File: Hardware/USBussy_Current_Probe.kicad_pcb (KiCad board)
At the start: 4 copper layers, 33.5 x 30 mm, 29 parts, among them J1 USB_C_Receptacle_USB2.0, J2 Mobo header, J3 CFG_OPT1, J4 CFG_COM, J5 CFG_OPT2, J6 USB_A, J7 Jumper holder, J8 MEAS, Q1 RE1C002UN, Q2 RE1C002UN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

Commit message: Add texts on board and export
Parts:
- added SYM1: ~, leptunKicadLib:AMOGUS, B.Cu at (36.6, 83.1)
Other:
- board text added: "USBussy Current Probe Alex Voinea https://github.com/leptun"
- board text added: "rev ${REVISION} ${ISSUE_DATE}"
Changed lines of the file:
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@@
       (plot_on_all_layers_selection 0x0000000_00000000)
       (disableapertmacros false)
-      (usegerberextensions false)
-      (usegerberattributes true)
-      (usegerberadvancedattributes true)
-      (creategerberjobfile true)
+      (usegerberextensions true)
+      (usegerberattributes false)
+      (usegerberadvancedattributes false)
+      (creategerberjobfile false)
       (dashed_line_dash_ratio 12.000000)
       (dashed_line_gap_ratio 3.000000)
@@
       (plotinvisibletext false)
       (sketchpadsonfab false)
-      (subtractmaskfromsilk false)
+      (subtractmaskfromsilk true)
       (outputformat 1)
       (mirror false)
-      (drillshape 1)
+      (drillshape 0)
       (scaleselection 1)
-      (outputdirectory "")
+      (outputdirectory "out/")
     )
   )
@@
     (fp_line (start 1 0.625) (end -1 0.625)
       (stroke (width 0.1) (type solid)) (layer "F.Fab"))
-    (pad "1" smd roundrect (at -0.9125 0 180) (size 1.025 1.4) (layers "F.Cu" "F.Paste" "F.Mask") (roundrect_rratio 0.243902)
+    (pad "1" smd roundrect (at -0.9125 0 180) (size 1.025 1.4) (layers "F.Cu" "F.Paste" "F.Mask") (roundrect_rratio 0.243902439)
       (net 6 "Net-(D2-A)") (pintype "passive"))
-    (pad "2" smd roundrect (at 0.9125 0 180) (size 1.025 1.4) (layers "F.Cu" "F.Paste" "F.Mask") (roundrect_rratio 0.243902)
+    (pad "2" smd roundrect (at 0.9125 0 180) (size 1.025 1.4) (layers "F.Cu" "F.Paste" "F.Mask") (roundrect_rratio 0.243902439)
       (net 1 "+5V") (pintype "passive"))
     (model "${KICAD6_3DMODEL_DIR}/Resistor_SMD.3dshapes/R_0805_2012Metric.wrl"
@@
     (fp_line (start 1 0.625) (end -1 0.625)
       (stroke (width 0.1) (type solid)) (layer "F.Fab"))
-    (pad "1" smd roundrect (at -0.9125 0 180) (size 1.025 1.4) (layers "F.Cu" "F.Paste" "F.Mask") (roundrect_rratio 0.243902)
+    (pad "1" smd roundrect (at -0.9125 0 180) (size 1.025 1.4) (layers "F.Cu" "F.Paste" "F.Mask") (roundrect_rratio 0.243902439)
       (net 4 "Net-(D1-A)") (pintype "passive"))
-    (pad "2" smd roundrect (at 0.9125 0 180) (size 1.025 1.4) (layers "F.Cu" "F.Paste" "F.Mask") (roundrect_rratio 0.243902)
+    (pad "2" smd roundrect (at 0.9125 0 180) (size 1.025 1.4) (layers "F.Cu" "F.Paste" "F.Mask") (roundrect_rratio 0.243902439)
       (net 1 "+5V") (pintype "passive"))
     (model "${KICAD6_3DMODEL_DIR}/Resistor_SMD.3dshapes/R_0805_2012Metric.wrl"
@@
     (fp_line (start 1.6 1.25) (end -1.6 1.25)
       (stroke (width 0.1) (type solid)) (layer "F.Fab"))
-    (pad "1" smd roundrect (at -1.475 0 180) (size 1.15 2.7) (layers "F.Cu" "F.Paste" "F.Mask") (roundrect_rratio 0.217391)
+    (pad "1" smd roundrect (at -1.475 0 180) (size 1.15 2.7) (layers "F.Cu" "F.Paste" "F.Mask") (roundrect_rratio 0.2173913043)
       (net 2 "GND") (pintype "passive"))
-    (pad "2" smd roundrect (at 1.475 0 180) (size 1.15 2.7) (layers "F.Cu" "F.Paste" "F.Mask") (roundrect_rratio 0.217391)
+    (pad "2" smd roundrect (at 1.475 0 180) (size 1.15 2.7) (layers "F.Cu" "F.Paste" "F.Mask") (roundrect_rratio 0.2173913043)
       (net 7 "/USB_C_VBUS") (pintype "passive"))
     (model "${KICAD6_3DMODEL_DIR}/Capacitor_SMD.3dshapes/C_1210_3225Metric.wrl"
@@
     )
   )
+  (footprint "leptunKicadLib:AMOGUS" (layer "B.Cu")
+    (at 36.6014 83.0834 -90)
+    (property "Sheetfile" "USBussy_Current_Probe.kicad_sch")
+    (property "Sheetname" "")
+    (property "Sim.Enable" "0")
+    (property "exclude_from_bom" "")
+    (property "ki_description" "Open Hardware logo, small")
+    (property "ki_keywords" "Logo")
+    (attr through_hole exclude_from_bom)
+    (fp_text reference "SYM1" (at 0 -0.5 -270) (layer "B.SilkS") hide
+        (effects (font (size 1 1) (thickness 0.15)) (justify mirror))
+    )
+    (fp_text value "~" (at 0 0.5 -270) (layer "B.Fab")
+        (effects (font (size 1 1) (thickness 0.15)) (justify mirror))
+    )
+    (fp_curve (pts (xy -4.990555 -4.274239) (xy -4.479356 -3.251843) (xy -4.452111 -1.799887) (xy -4.270555 -0.674239))
+      (stroke (width 0.2) (type solid)) (layer "B.SilkS"))
+    (fp_curve (pts (xy -4.270555 -0.674239) (xy -4.025142 0.84732) (xy -3.680852 2.332061) (xy -3.230555 3.805761))
+      (stroke (width 0.2) (type solid)) (layer "B.SilkS"))
+    (fp_curve (pts (xy -3.870555 -5.634239) (xy -7.87736 -6.404779) (xy -8.612551 -3.469351) (xy -4.990555 -4.274239))
+      (stroke (width 0.2) (type solid)) (layer "B.SilkS"))
+    (fp_curve (pts (xy -3.230555 3.805761) (xy -3.075315 4.313819) (xy -2.616498 6.952463) (xy -1.550555 7.005761))
+      (stroke (width 0.2) (type solid)) (layer "B.SilkS"))
+    (fp_curve (pts (xy -2.271776 4.382116) (xy -2.269771 4.961755) (xy -1.098997 5.53735) (xy 0.069772 5.533306))
+      (stroke (width 0.2) (type solid)) (layer "B.SilkS"))
+    (fp_curve (pts (xy -1.550555 7.005761) (xy 0.209624 7.09377) (xy 0.753252 7.074619) (xy 2.049445 6.685761))
+      (stroke (width 0.2) (type solid)) (layer "B.SilkS"))
+    (fp_curve (pts (xy -0.830555 -6.514239) (xy -0.961599 -4.941714) (xy 0.912248 -5.749496) (xy 1.169445 -5.314239))
+      (stroke (width 0.2) (type solid)) (layer "B.SilkS"))
+    (fp_curve (pts (xy 0.06175 3.214751) (xy -1.107019 3.218795) (xy -2.273782 3.802477) (xy -2.271776 4.382116))
+      (stroke (width 0.2) (type solid)) (layer "B.SilkS"))
+    (fp_curve (pts (xy 0.069772 5.533306) (xy 1.238541 5.529262) (xy 2.405304 4.945579) (xy 2.403298 4.365941))
+      (stroke (width 0.2) (type solid)) (layer "B.SilkS"))
+    (fp_curve (pts (xy 0.449445 -2.114239) (xy -5.606765 -1.357213) (xy -0.20818 -4.929937) (xy -3.870555 -5.634239))
+      (stroke (width 0.2) (type solid)) (layer "B.SilkS"))
+    (fp_curve (pts (xy 1.089445 -2.434239) (xy 0.894047 -2.297461) (xy 0.686117 -2.143823) (xy 0.449445 -2.114239))
+      (stroke (width 0.2) (type solid)) (layer "B.SilkS"))
+    (fp_curve (pts (xy 1.169445 -5.314239) (xy 1.353719 -5.002391) (xy 1.746386 -2.894098) (xy 1.089445 -2.434239))
+      (stroke (width 0.2) (type solid)) (layer "B.SilkS"))
+    (fp_curve (pts (xy 1.489445 -7.154239) (xy 1.341106 -7.159025) (xy -0.768282 -7.261512) (xy -0.830555 -6.514239))
+      (stroke (width 0.2) (type solid)) (layer "B.SilkS"))
+    (fp_curve (pts (xy 2.049445 6.685761) (xy 3.34614 6.296752) (xy 3.868407 3.776144) (xy 3.969445 2.765761))
+      (stroke (width 0.2) (type solid)) (layer "B.SilkS"))
+    (fp_curve (pts (xy 2.403298 4.365941) (xy 2.401293 3.786302) (xy 1.230519 3.210707) (xy 0.06175 3.214751))
+      (stroke (width 0.2) (type solid)) (layer "B.SilkS"))
+    (fp_curve (pts (xy 2.449445 -6.994239) (xy 2.131331 -7.057862) (xy 1.813691 -7.14378) (xy 1.489445 -7.154239))
+      (stroke (width 0.2) (type solid)) (layer "B.SilkS"))
+    (fp_curve (pts (xy 3.969445 2.765761) (xy 4.070589 1.754319) (xy 4.149047 0.740451) (xy 4.209445 -0.274239))
+      (stroke (width 0.2) (type solid)) (layer "B.SilkS"))
+    (fp_curve (pts (xy 4.209445 -0.274239) (xy 4.282401 -1.499896) (xy 4.369445 -2.726414) (xy 4.369445 -3.954239))
+      (stroke (width 0.2) (type solid)) (layer "B.SilkS"))
+    (fp_curve (pts (xy 4.369445 -3.954239) (xy 4.369445 -5.989742) (xy 4.386831 -6.606762) (xy 2.449445 -6.994239))
+      (stroke (width 0.2) (type solid)) (layer "B.SilkS"))
+  )
   (gr_rect (start 29.083 58.039) (end 62.611 88.011)
     (stroke (width 0.1) (type default)) (fill none) (layer "Edge.Cuts"))
+  (gr_text "rev ${REVISION}\n${ISSUE_DATE}" (at 41.6052 86.8426) (layer "B.SilkS")
+    (effects (font (size 0.8 0.8) (thickness 0.12)) (justify left bottom mirror))
+  )
+  (gr_text "USBussy Current Probe\nAlex Voinea\nhttps://github.com/leptun" (at 62.1792 87.503) (layer "B.SilkS")
+    (effects (font (size 0.8 0.8) (thickness 0.12)) (justify left bottom mirror))
+  )
   (segment (start 42.423 64.6756) (end 42.423 62.616) (width 0.5) (layer "F.Cu") (net 1))
   (segment (start 51.369 68.707) (end 51.369 66.6598) (width 0.5) (layer "F.Cu") (net 1))

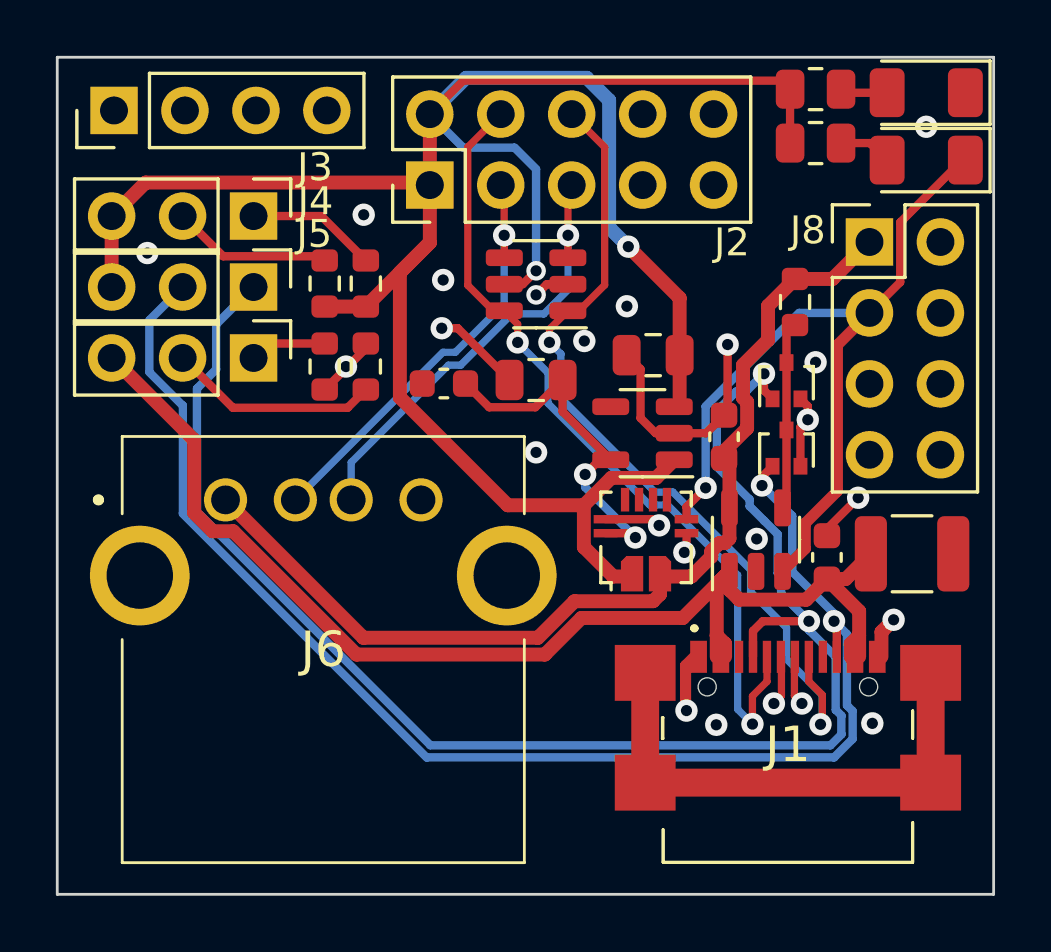
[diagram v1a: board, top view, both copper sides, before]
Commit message: Add pinout on silkscreen
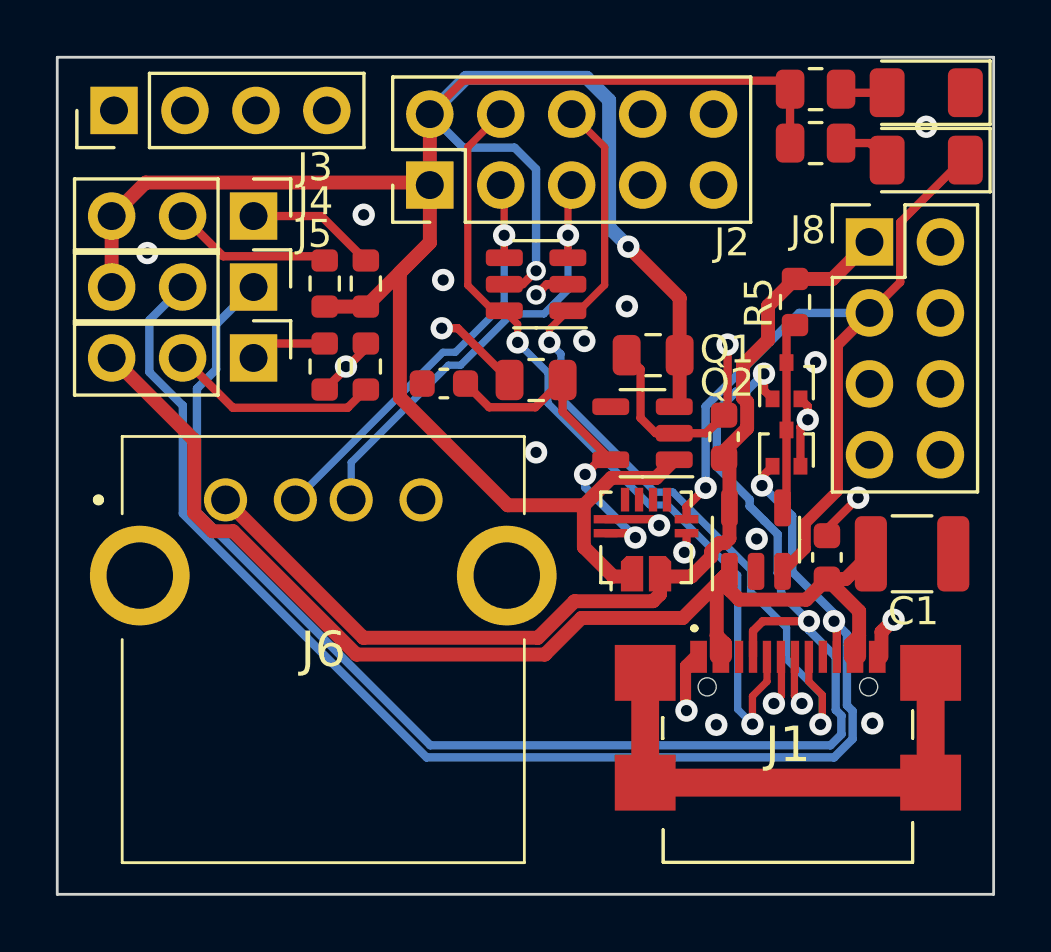
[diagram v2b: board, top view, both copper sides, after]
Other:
- board text added: "3.3V"
- board text added: "5V + - GND"
- board text added: "CC1"
- board text added: "CC2"
- board text added: "FAULT"
- board text added: "GND"
- board text added: "MEAS"
- board text added: "VBUS"
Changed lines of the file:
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@@
     (property "ki_keywords" "transistor NMOS N-MOS N-MOSFET")
     (attr smd)
-    (fp_text reference "Q2" (at -0.0254 0 90) (layer "B.SilkS")
-        (effects (font (size 1 1) (thickness 0.15)) (justify mirror))
+    (fp_text reference "Q2" (at 2.3368 -2.1336) (layer "F.SilkS")
+        (effects (font (size 1 1) (thickness 0.15)))
     )
     (fp_text value "RE1C002UN" (at 0 2.25 90) (layer "F.Fab")
@@
     (property "ki_keywords" "capacitor cap")
     (attr smd)
-    (fp_text reference "C3" (at 0 0 -270) (layer "B.SilkS")
+    (fp_text reference "C3" (at 0 0.1778 -270) (layer "B.SilkS")
         (effects (font (size 1 1) (thickness 0.15)) (justify mirror))
     )
@@
     (property "ki_keywords" "usb ethernet sim card video")
     (attr smd)
-    (fp_text reference "U2" (at 0 0 270) (layer "B.SilkS")
+    (fp_text reference "U2" (at 0 0) (layer "B.SilkS")
         (effects (font (size 1 1) (thickness 0.15)) (justify mirror))
     )
@@
     (property "ki_keywords" "R resistor")
     (attr smd)
-    (fp_text reference "R5" (at 0 0 -270) (layer "B.SilkS")
-        (effects (font (size 1 1) (thickness 0.15)) (justify mirror))
+    (fp_text reference "R5" (at 0.0254 1.2954 90) (layer "F.SilkS")
+        (effects (font (size 1 1) (thickness 0.15)))
     )
     (fp_text value "10K" (at 0 1.43 90) (layer "F.Fab")
@@
     (property "ki_keywords" "transistor NMOS N-MOS N-MOSFET")
     (attr smd)
-    (fp_text reference "Q1" (at -0.0254 0 90) (layer "B.SilkS")
-        (effects (font (size 1 1) (thickness 0.15)) (justify mirror))
+    (fp_text reference "Q1" (at 1.1176 -2.1336 180) (layer "F.SilkS")
+        (effects (font (size 1 1) (thickness 0.15)))
     )
     (fp_text value "RE1C002UN" (at 0 2.25 90) (layer "F.Fab")
@@
     (property "ki_keywords" "capacitor cap")
     (attr smd)
-    (fp_text reference "C1" (at 0 0 -360) (layer "B.SilkS")
-        (effects (font (size 1 1) (thickness 0.15)) (justify mirror))
+    (fp_text reference "C1" (at -0.0508 -2.0574) (layer "F.SilkS")
+        (effects (font (size 1 1) (thickness 0.15)))
     )
     (fp_text value "22uF" (at 0 2.3) (layer "F.Fab")
@@
   (gr_rect (start 29.083 58.039) (end 62.611 88.011)
     (stroke (width 0.1) (type default)) (fill none) (layer "Edge.Cuts"))
+  (gr_text "FAULT" (at 57.0992 67.183) (layer "B.SilkS")
+    (effects (font (size 1 1) (thickness 0.15)) (justify left mirror))
+  )
+  (gr_text "3.3V" (at 57.0738 69.723) (layer "B.SilkS")
+    (effects (font (size 1 1) (thickness 0.15)) (justify left mirror))
+  )
+  (gr_text "CC2" (at 33.5788 71.5772 90) (layer "B.SilkS")
+    (effects (font (size 1 1) (thickness 0.15)) (justify mirror))
+  )
+  (gr_text "VBUS" (at 31.0388 71.8312 90) (layer "B.SilkS")
+    (effects (font (size 1 1) (thickness 0.15)) (justify mirror))
+  )
+  (gr_text "5V +  - GND" (at 46.9138 64.1604 180) (layer "B.SilkS")
+    (effects (font (size 1 1) (thickness 0.15)) (justify mirror))
+  )
   (gr_text "rev ${REVISION}\n${ISSUE_DATE}" (at 41.6052 86.8426) (layer "B.SilkS")
     (effects (font (size 0.8 0.8) (thickness 0.12)) (justify left bottom mirror))
   )
+  (gr_text "VBUS" (at 57.15 64.6684) (layer "B.SilkS")
+    (effects (font (size 1 1) (thickness 0.15)) (justify left mirror))
+  )
+  (gr_text "CC1" (at 36.1442 71.5518 90) (layer "B.SilkS")
+    (effects (font (size 1 1) (thickness 0.15)) (justify mirror))
+  )
   (gr_text "USBussy Current Probe\nAlex Voinea\nhttps://github.com/leptun" (at 62.1792 87.503) (layer "B.SilkS")
     (effects (font (size 0.8 0.8) (thickness 0.12)) (justify left bottom mirror))
   )
+  (gr_text "GND" (at 60.7568 73.152 90) (layer "B.SilkS")
+    (effects (font (size 1 1) (thickness 0.15)) (justify left mirror))
+  )
+  (gr_text "MEAS" (at 57.0992 72.2884) (layer "B.SilkS")
+    (effects (font (size 1 1) (thickness 0.15)) (justify left mirror))
+  )
   (segment (start 42.423 64.6756) (end 42.423 62.616) (width 0.5) (layer "F.Cu") (net 1))
